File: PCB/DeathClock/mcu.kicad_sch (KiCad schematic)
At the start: 9 parts, among them J1 Conn_01x05_Female, U1 STM32L010F4P6, Y1 Crystal

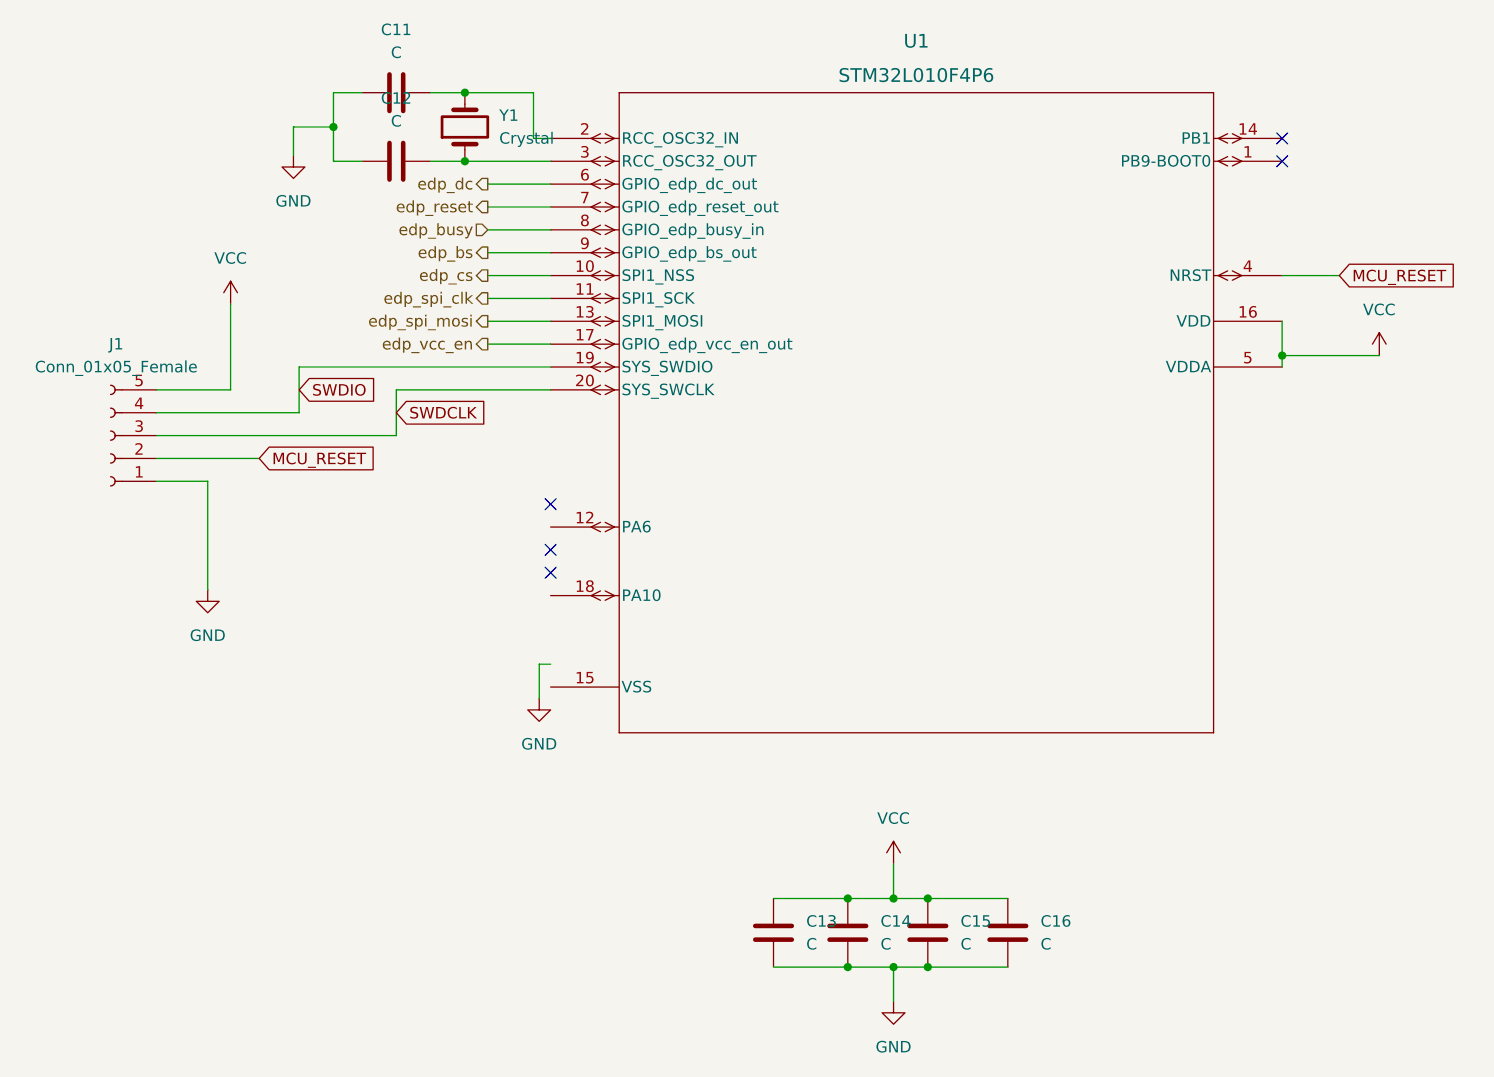
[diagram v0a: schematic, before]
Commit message: made the coin cell symbol 4 pins to make drc happy
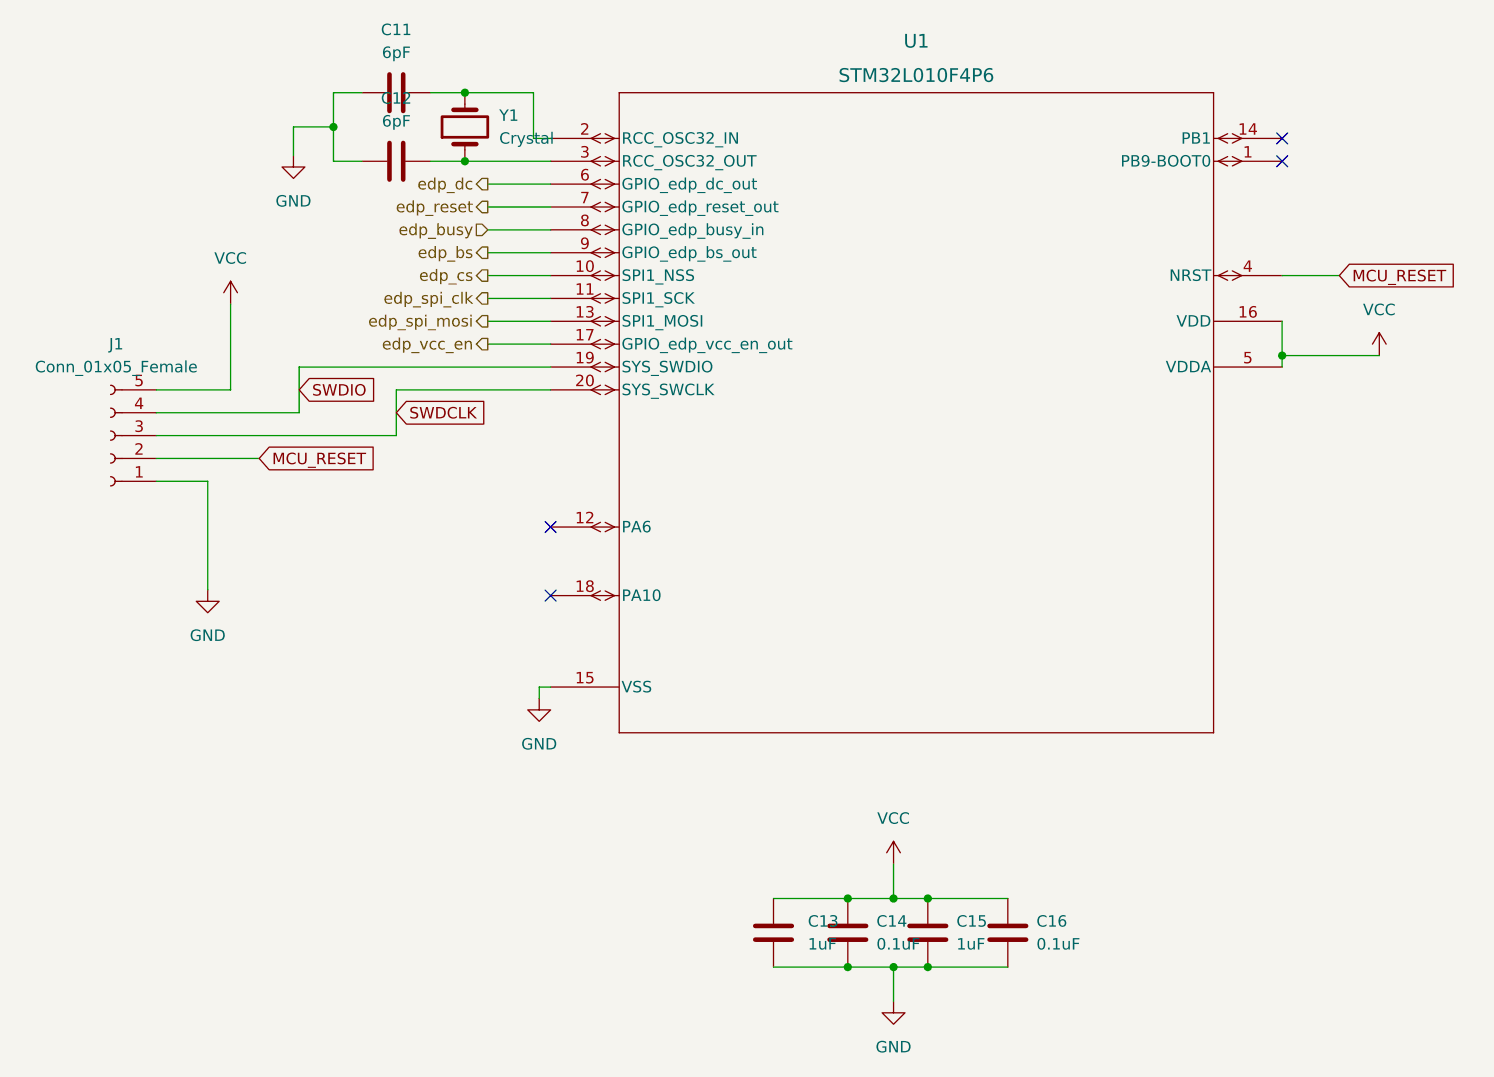
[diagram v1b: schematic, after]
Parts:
- C11, C12: value C -> 6pF
- C13, C15: value C -> 1uF
- C14, C16: value C -> 0.1uF
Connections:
- net GND: now also U1.15 (VSS)
- no-connect marks 5 -> 4
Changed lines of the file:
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@@
   (junction (at 137.795 128.27) (diameter 0) (color 0 0 0 0)
   )
-  (no_connect (at 104.775 76.835))
-  (no_connect (at 104.775 84.455))
-  (no_connect (at 104.775 81.915))
+  (no_connect (at 104.775 79.375))
+  (no_connect (at 104.775 86.995))
   (no_connect (at 186.055 38.735))
   (no_connect (at 186.055 36.195))
@@
     (stroke (width 0) (type default) (color 0 0 0 0))
   )
-  (wire (pts (xy 104.775 94.615) (xy 103.505 94.615))
+  (wire (pts (xy 104.775 97.155) (xy 103.505 97.155))
     (stroke (width 0) (type default) (color 0 0 0 0))
   )
@@
     (stroke (width 0) (type default) (color 0 0 0 0))
   )
-  (wire (pts (xy 103.505 94.615) (xy 103.505 98.425))
+  (wire (pts (xy 103.505 97.155) (xy 103.505 98.425))
     (stroke (width 0) (type default) (color 0 0 0 0))
   )
@@
   (symbol (lib_id "Device:C") (at 146.685 124.46 180) (unit 1)
     (in_bom yes) (on_board yes) (fields_autoplaced)
-    (property "Reference" "C15" (id 0) (at 150.3164 123.1899 0)
-      (effects (font (size 1.27 1.27)) (justify right))
-    )
-    (property "Value" "C" (id 1) (at 150.3164 125.7299 0)
+    (property "Reference" "C15" (id 0) (at 149.86 123.1899 0)
+      (effects (font (size 1.27 1.27)) (justify right))
+    )
+    (property "Value" "1uF" (id 1) (at 149.86 125.7299 0)
       (effects (font (size 1.27 1.27)) (justify right))
     )
@@
     (in_bom yes) (on_board yes) (fields_autoplaced)
     (property "Reference" "C11" (id 0) (at 87.63 24.13 90))
-    (property "Value" "C" (id 1) (at 87.63 26.67 90))
+    (property "Value" "6pF" (id 1) (at 87.63 26.67 90))
     (property "Footprint" "Capacitor_SMD:C_0402_1005Metric_Pad0.74x0.62mm_HandSolder" (id 2) (at 91.44 30.1498 0)
       (effects (font (size 1.27 1.27)) hide)
@@
   (symbol (lib_id "Device:C") (at 137.795 124.46 180) (unit 1)
     (in_bom yes) (on_board yes) (fields_autoplaced)
-    (property "Reference" "C14" (id 0) (at 141.4264 123.1899 0)
-      (effects (font (size 1.27 1.27)) (justify right))
-    )
-    (property "Value" "C" (id 1) (at 141.4264 125.7299 0)
+    (property "Reference" "C14" (id 0) (at 140.97 123.1899 0)
+      (effects (font (size 1.27 1.27)) (justify right))
+    )
+    (property "Value" "0.1uF" (id 1) (at 140.97 125.7299 0)
       (effects (font (size 1.27 1.27)) (justify right))
     )
@@
     (in_bom yes) (on_board yes) (fields_autoplaced)
     (property "Reference" "C12" (id 0) (at 87.63 31.75 90))
-    (property "Value" "C" (id 1) (at 87.63 34.29 90))
+    (property "Value" "6pF" (id 1) (at 87.63 34.29 90))
     (property "Footprint" "Capacitor_SMD:C_0402_1005Metric_Pad0.74x0.62mm_HandSolder" (id 2) (at 91.44 37.7698 0)
       (effects (font (size 1.27 1.27)) hide)
@@
   (symbol (lib_id "Device:C") (at 129.54 124.46 180) (unit 1)
     (in_bom yes) (on_board yes) (fields_autoplaced)
-    (property "Reference" "C13" (id 0) (at 133.1714 123.1899 0)
-      (effects (font (size 1.27 1.27)) (justify right))
-    )
-    (property "Value" "C" (id 1) (at 133.1714 125.7299 0)
+    (property "Reference" "C13" (id 0) (at 133.35 123.1899 0)
+      (effects (font (size 1.27 1.27)) (justify right))
+    )
+    (property "Value" "1uF" (id 1) (at 133.35 125.7299 0)
       (effects (font (size 1.27 1.27)) (justify right))
     )
@@
   (symbol (lib_id "Device:C") (at 155.575 124.46 180) (unit 1)
     (in_bom yes) (on_board yes) (fields_autoplaced)
-    (property "Reference" "C16" (id 0) (at 159.2064 123.1899 0)
-      (effects (font (size 1.27 1.27)) (justify right))
-    )
-    (property "Value" "C" (id 1) (at 159.2064 125.7299 0)
-      (effects (font (size 1.27 1.27)) (justify right))
-    )
+    (property "Reference" "C16" (id 0) (at 158.75 123.1899 0)
+      (effects (font (size 1.27 1.27)) (justify right))
+    )
+    (property "Value" "0.1uF" (id 1) (at 158.75 125.7299 0)
+      (effects (font (size 1.27 1.27)) (justify right))
+    )
